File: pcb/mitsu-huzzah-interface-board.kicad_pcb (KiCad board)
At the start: 2 copper layers, 25.9 x 49.8 mm, 11 parts, among them J1 AIRCON, J2 DEBUG, SW1 KMR2, U1 TXB0102DCUT

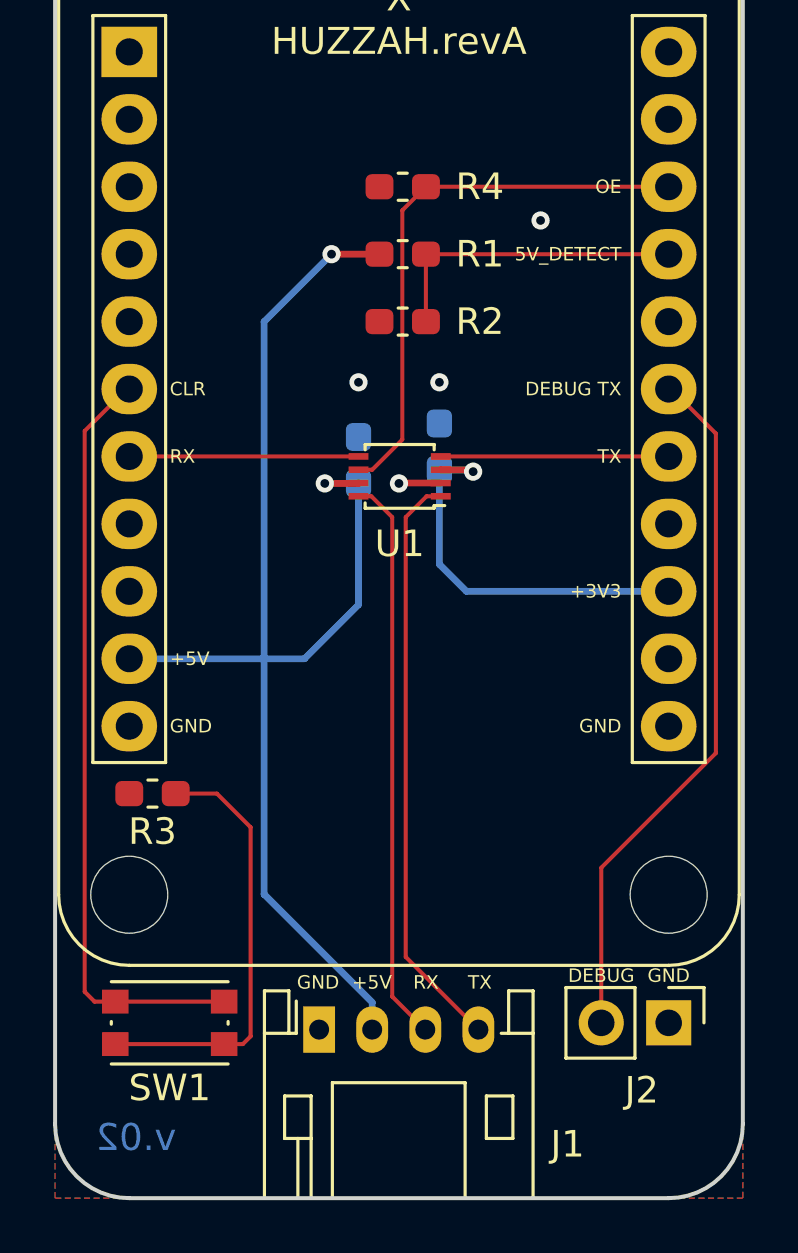
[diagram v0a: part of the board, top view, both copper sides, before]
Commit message: Update the PCB with a bigger level shifter
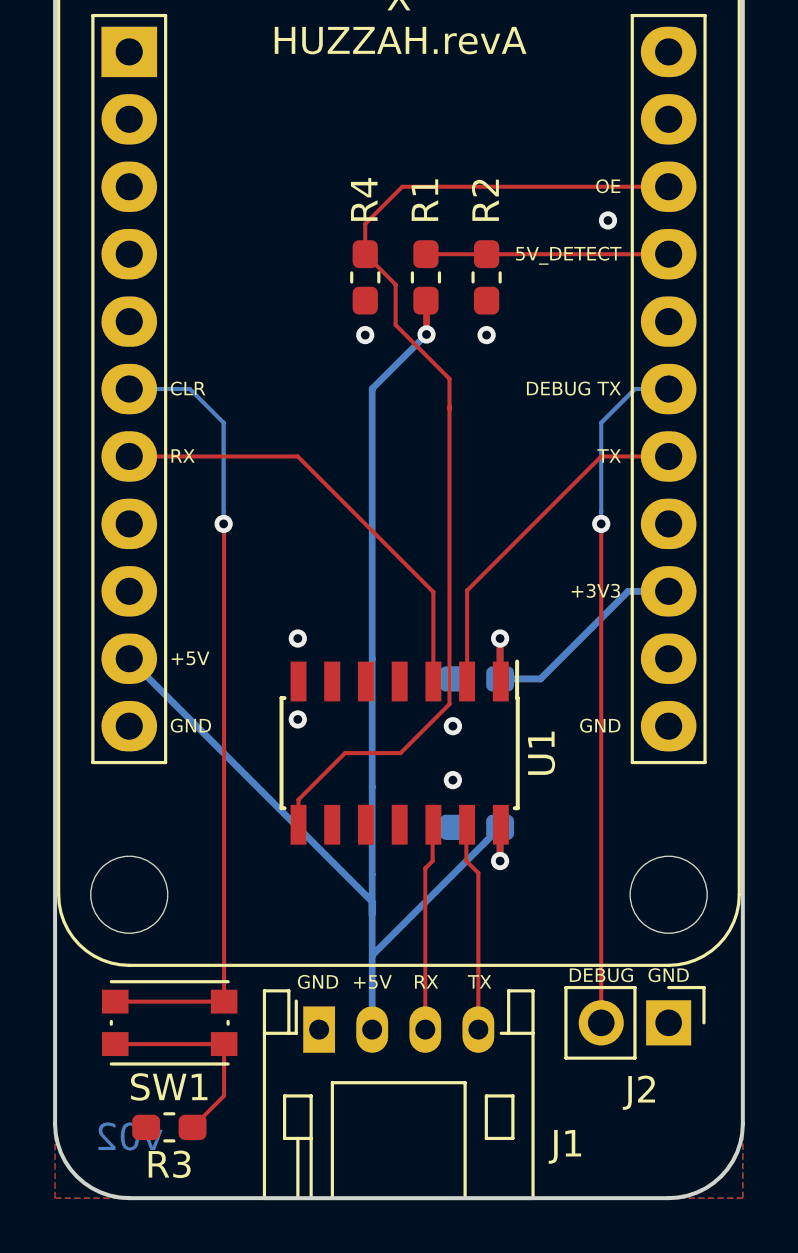
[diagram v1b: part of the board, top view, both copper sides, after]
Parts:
- U1: value TXB0102DCUT -> TXB0104DR; footprint Package_SO:VSSOP-8_2.4x2.1mm_P0.5mm -> Package_SO:SOIC-14_3.9x8.7mm_P1.27mm
- moved C2 14.5 mm to (145.5, 112.0), turned to 180 degrees
- moved R3 12.6 mm to (133.9, 123.3)
- moved U1 10.4 mm to (142.6, 109.2), turned to 270 degrees
- moved C1 8.86 mm to (145.5, 106.4), turned to 180 degrees
- moved R4 3.70 mm to (141.3, 91.3), turned to 270 degrees
- moved R2 3.57 mm to (145.9, 91.3), turned to 270 degrees
- moved R1 1.24 mm to (143.6, 91.3), turned to 90 degrees
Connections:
- U1 pad 1: /TX0*_5V -> +3V3
- U1 pad 2: GND -> /TX0*
- U1 pad 3: +3V3 -> /RX0*
- U1 pad 4: /TX0* -> Net-(U1-Pad4)
- U1 pad 5: /RX0* -> Net-(U1-Pad5)
- U1 pad 6: /OE -> Net-(U1-Pad6)
- U1 pad 7: +5V -> GND
- U1 pad 8: /RX0*_5V -> /OE
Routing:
- net /OE: track 21.2 -> 39.7 mm
- net /TX0*_5V: track 22.1 -> 7.91 mm
- net /RX0*_5V: track 21.4 -> 7.87 mm
- net Net-(R3-Pad1): track 16.4 -> 7.73 mm
- net /RX0*: track 9.00 -> 16.9 mm
- net +3V3: track 15.2 -> 10.9 mm
- net /TX0*: track 8.94 -> 13.1 mm
- net /5V_DET: track 11.7 -> 9.14 mm
- net GND: track 1.58 -> 0.00 mm, vias 4 -> 7
- net /CLEAR: track 28.9 -> 30.1 mm, vias 0 -> 1
- net +5V: track 50.4 -> 51.2 mm
- net /TX1: track 26.5 -> 25.7 mm, vias 0 -> 1
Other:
- board text added: "v02"
- board text removed: "v.02"

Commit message: Update voltage divider resistor values
2K2/3K3 gives a 3V output too, and I didn't want to wait for stock on
the old values.
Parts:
- R1: value 3K9 -> 2K2
- R2: value 6K8 -> 3K3
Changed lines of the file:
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@@
       (effects (font (size 1 1) (thickness 0.15)))
     )
-    (fp_text value 6K8 (at 3.951 0 270) (layer F.Fab)
+    (fp_text value 3K3 (at 3.951 0 270) (layer F.Fab)
       (effects (font (size 1 1) (thickness 0.15)))
     )
@@
       (effects (font (size 1 1) (thickness 0.15)))
     )
-    (fp_text value 3K9 (at -3.951 0 90) (layer F.Fab)
+    (fp_text value 2K2 (at -3.951 0 90) (layer F.Fab)
       (effects (font (size 1 1) (thickness 0.15)))
     )

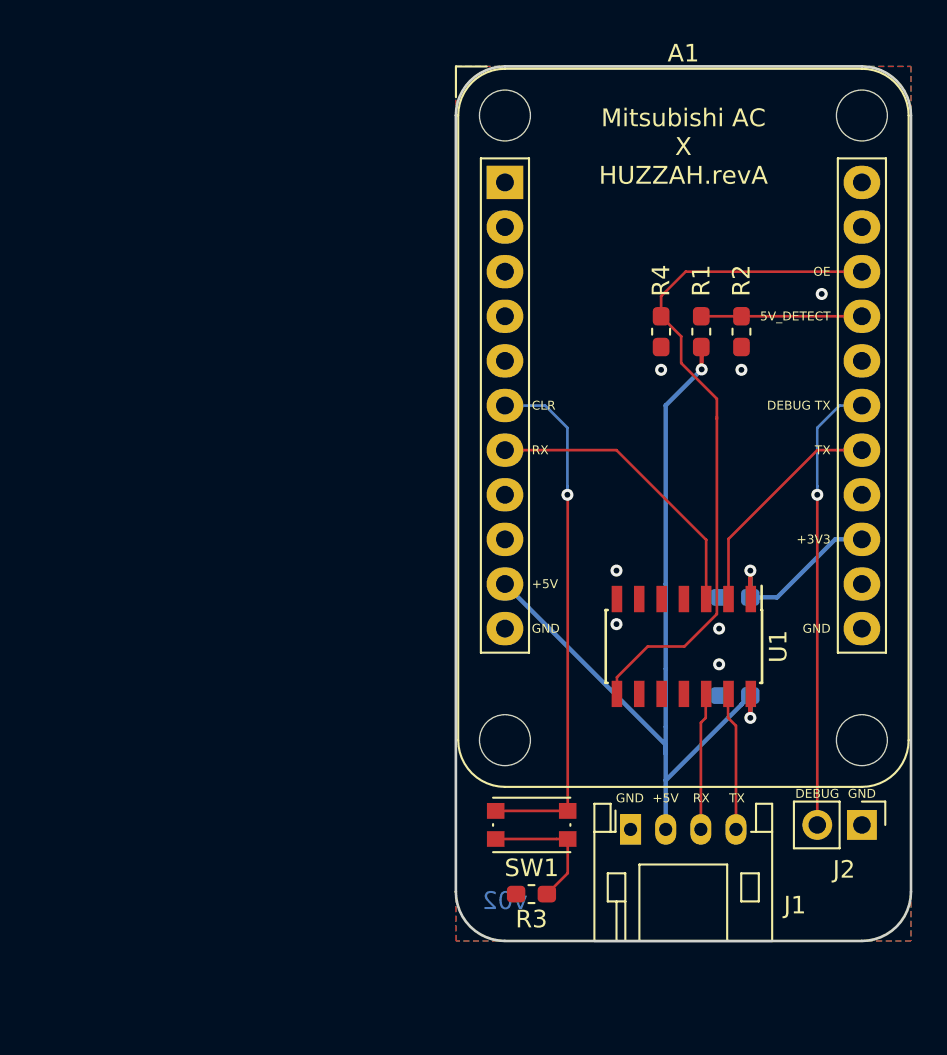
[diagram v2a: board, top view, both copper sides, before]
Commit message: Change design to a completely custom PCB
No more adafruit HUZZAH, instead build a custom PCB for an ESP-12S module.
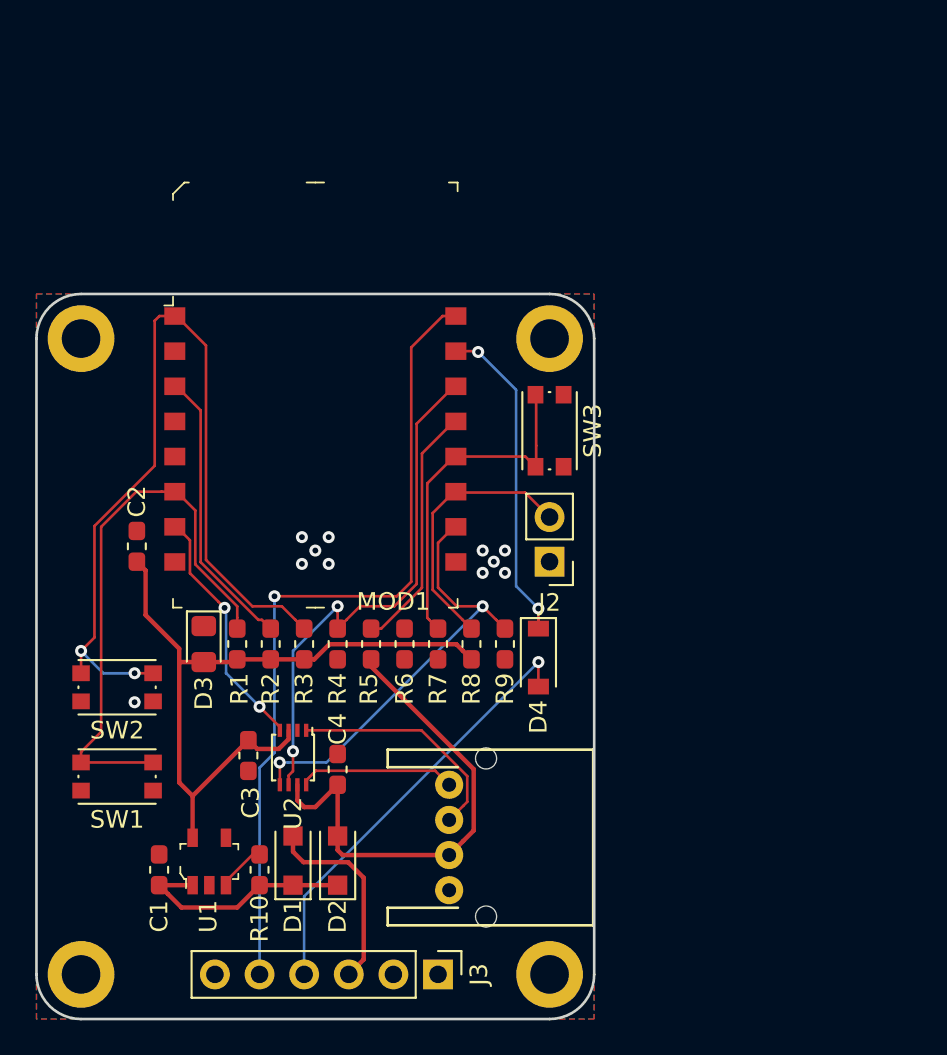
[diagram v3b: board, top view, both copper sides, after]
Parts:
- removed A1: HUZZAH, mitsu-huzzah-interface-footprints:Adafruit_HUZZAH_ESP8266_breakout_revA_WithMountingHoles
- added C3: 0.1uF, Capacitor_SMD:C_0603_1608Metric_Pad1.05x0.95mm_HandSolder, F.Cu at (117.8, 115.4)
- added C4: 0.1uF, Capacitor_SMD:C_0603_1608Metric_Pad1.05x0.95mm_HandSolder, F.Cu at (122.9, 116.2)
- added D1: MBR120, Diode_SMD:D_SOD-123F, F.Cu at (120.3, 121.4)
- added D2: MBR120, Diode_SMD:D_SOD-123F, F.Cu at (122.9, 121.4)
- added D3: RED, LED_SMD:LED_0805_2012Metric_Pad1.15x1.40mm_HandSolder, F.Cu at (115.2, 109.1)
- added D4: MMSD914, Diode_SMD:D_SOD-123, F.Cu at (134.3, 109.9)
- added J3: FTDI, Connector_PinHeader_2.54mm:PinHeader_1x06_P2.54mm_Vertical, F.Cu at (128.6, 127.9)
- added MOD1: 2491, mitsu-huzzah-interface-footprints:WIFI_Module_ESP8266_2491, F.Cu at (121.6, 97.4)
- added R10: 10K, Resistor_SMD:R_0603_1608Metric_Pad1.05x0.95mm_HandSolder, F.Cu at (118.4, 121.9)
- added R5: 2K2, Resistor_SMD:R_0603_1608Metric_Pad1.05x0.95mm_HandSolder, F.Cu at (124.8, 109.1)
- added R6: 3K3, Resistor_SMD:R_0603_1608Metric_Pad1.05x0.95mm_HandSolder, F.Cu at (126.7, 109.1)
- added R7: 1K, Resistor_SMD:R_0603_1608Metric_Pad1.05x0.95mm_HandSolder, F.Cu at (128.6, 109.1)
- added R8: 10K, Resistor_SMD:R_0603_1608Metric_Pad1.05x0.95mm_HandSolder, F.Cu at (130.5, 109.1)
- added R9: 10K, Resistor_SMD:R_0603_1608Metric_Pad1.05x0.95mm_HandSolder, F.Cu at (132.4, 109.1)
- added REF**: MountingHole_2.2mm_M2_DIN965_Pad, MountingHole:MountingHole_2.2mm_M2_DIN965_Pad, F.Cu at (108.3, 127.9)
- added REF**: MountingHole_2.2mm_M2_DIN965_Pad, MountingHole:MountingHole_2.2mm_M2_DIN965_Pad, F.Cu at (134.9, 127.9)
- added REF**: MountingHole_2.2mm_M2_DIN965_Pad, MountingHole:MountingHole_2.2mm_M2_DIN965_Pad, F.Cu at (134.9, 91.7)
- added REF**: MountingHole_2.2mm_M2_DIN965_Pad, MountingHole:MountingHole_2.2mm_M2_DIN965_Pad, F.Cu at (108.3, 91.7)
- added SW2: KMR2, mitsu-huzzah-interface-footprints:SW_SPST_KMR2, F.Cu at (110.3, 111.5)
- added SW3: KMR2, mitsu-huzzah-interface-footprints:SW_SPST_KMR2, F.Cu at (134.9, 96.9)
- added U2: TXB0102DCU, Package_SO:VSSOP-8_2.4x2.1mm_P0.5mm, F.Cu at (120.3, 115.5)
- C1, C2: value 0.1uF -> 10uF; moved to F.Cu
- J1: footprint Connector_JST:JST_PH_S4B-PH-K_1x04_P2.00mm_Horizontal -> mitsu-huzzah-interface-footprints:S04B-PASK-2
- R1: value 2K2 -> 10K
- R2: value 3K3 -> 10K
- R3, R4: value 1K -> 10K
- SW1: footprint Button_Switch_SMD:SW_SPST_KMR2 -> mitsu-huzzah-interface-footprints:SW_SPST_KMR2
- U1: value TXB0104DR -> AP2112K-3.3TRG1; footprint Package_SO:SOIC-14_3.9x8.7mm_P1.27mm -> digikey-footprints:SOT-753
- moved C1 36.3 mm to (112.7, 121.9), turned to 90 degrees
- moved C2 35.1 mm to (111.4, 103.5), turned to 90 degrees
- moved R2 32.2 mm to (119.1, 109.1), turned to 90 degrees
- moved R1 31.8 mm to (117.2, 109.1)
- moved U1 29.7 mm to (115.6, 121.5), turned to 0 degrees
- moved R4 25.6 mm to (122.9, 109.1)
- moved SW1 23.8 mm to (110.3, 116.6)
- moved J2 23.3 mm to (134.9, 104.4), turned to 180 degrees
- moved R3 19.2 mm to (121.0, 109.1), turned to 90 degrees
- moved J1 10.3 mm to (129.2, 120.1), turned to 270 degrees
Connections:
- C1 pad 1: +3V3 -> Net-(C1-Pad1)
- C2 pad 1: +5V -> +3V3
- J1 pad 3: /RX0*_5V -> /RXD0*_5V
- J1 pad 4: /TX0*_5V -> /TXD0*_5V
- J2 pad 2: /TX1 -> /GPIO2
- R1 pad 1: +5V -> +3V3
- R1 pad 2: /5V_DET -> /CLEAR
- R2 pad 1: /5V_DET -> +3V3
- R2 pad 2: GND -> /CH_PD
- R3 pad 1: Net-(R3-Pad1) -> +3V3
- R3 pad 2: GND -> /RESET
- SW1 pad 1: Net-(R3-Pad1) -> GND
- U1 pad 1: +3V3 -> Net-(C1-Pad1)
- U1 pad 2: /TX0* -> GND
- U1 pad 3: /RX0* -> Net-(R10-Pad2)
- U1 pad 4: Net-(U1-Pad4) -> (no net)
- U1 pad 5: Net-(U1-Pad5) -> +3V3
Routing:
- net /RESET: track 0.00 -> 49.6 mm, vias 0 -> 2
- net /FTDI_RX: track 0.00 -> 46.6 mm, vias 0 -> 1
- net +3V3: track 10.9 -> 42.2 mm, vias 1 -> 0
- net /TX1: track 25.7 -> 0.00 mm, vias 1 -> 0
- net /GPIO15: track 0.00 -> 25.2 mm, vias 0 -> 2
- net /FTDI_TX: track 0.00 -> 24.7 mm, vias 0 -> 1
- net +5V: track 51.2 -> 28.2 mm, vias 2 -> 0
- net /GPIO0: track 0.00 -> 19.7 mm
- net /RXD0: track 0.00 -> 19.1 mm, vias 0 -> 2
- net /RX0*: track 16.9 -> 0.00 mm
- net /CH_PD: track 0.00 -> 16.2 mm
- net /GPIO2: track 0.00 -> 15.5 mm
- net /GPIO13: track 0.00 -> 14.1 mm, vias 0 -> 2
- net /RXD0*_5V: track 0.00 -> 13.2 mm
- net Net-(C1-Pad1): track 0.00 -> 13.1 mm
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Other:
- board size 25.9 x 49.8 mm -> 31.8 x 41.3 mm
- board text removed: "+3V3"
- board text removed: "+5V"
- board text removed: "5V_DETECT"
- board text removed: "@dgoodlad"
- board text removed: "CLR"
- board text removed: "DEBUG"
- board text removed: "DEBUG TX"
- board text removed: "GND"
- board text removed: "Mitsubishi AC X HUZZAH.revA"
- board text removed: "OE"
- board text removed: "RX"
- board text removed: "TX"
- board text removed: "v02"
